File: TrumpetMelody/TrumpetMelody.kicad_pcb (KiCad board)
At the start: 2 copper layers, 76.2 x 68.6 mm, 81 parts, among them J1 USB_B_Micro, J2 Conn_01x05, J3 640456-3, J4 640456-3, SW1 SW_Push, U1 STM32F411RETx, U2 TLV62565DBVR, U3 MAX98357AETE_T, U4 MAX7375AXR805

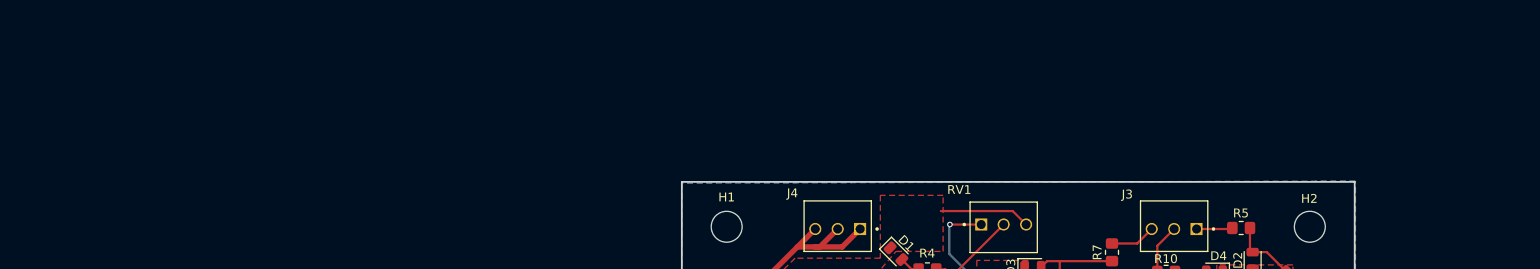
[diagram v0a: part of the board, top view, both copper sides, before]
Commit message: tbd list readded with things that need to be done
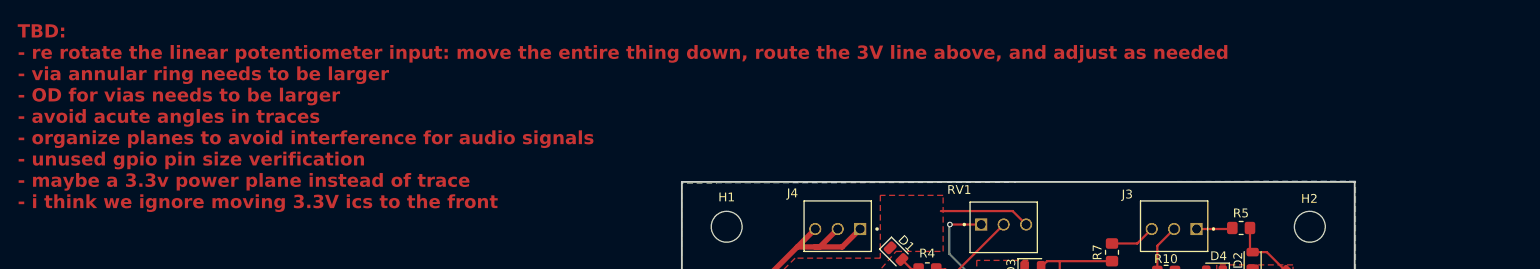
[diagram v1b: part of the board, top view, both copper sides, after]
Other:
- board text added: "TBD: - re rotate the linear potentiometer input: move the entire thing down, route the 3V line above, and adjust as needed - via annular ring needs to be larger - OD for vias needs to be larger - avoid acute angles in traces - organize planes to avoid interference for audio signals - unused gpio pin size verification - maybe a 3.3v power plane instead of trace - i think we ignore moving 3.3V ics 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"
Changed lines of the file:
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@@
   (gr_rect locked (start 147.32 45.72) (end 223.52 114.3)
     (stroke (width 0.2) (type default)) (fill none) (layer "Edge.Cuts"))
+  (gr_text "TBD:\n- re rotate the linear potentiometer input: move the entire thing down, route the 3V line above, and adjust as needed\n- via annular ring needs to be larger\n- OD for vias needs to be larger\n- avoid acute angles in traces\n- organize planes to avoid interference for audio signals\n- unused gpio pin size verification\n- maybe a 3.3v power plane instead of trace\n- i think we ignore moving 3.3V ics to the front" (at 72.105 48.87) (layer "F.Cu")
+    (effects (font (size 1.5 1.5) (thickness 0.3) bold) (justify left bottom))
+  )
   (gr_text "TMS" (at 185.301178 98.92878 -45) (layer "F.SilkS")
     (effects (font (size 0.635 0.635) (thickness 0.1)) (justify left bottom))

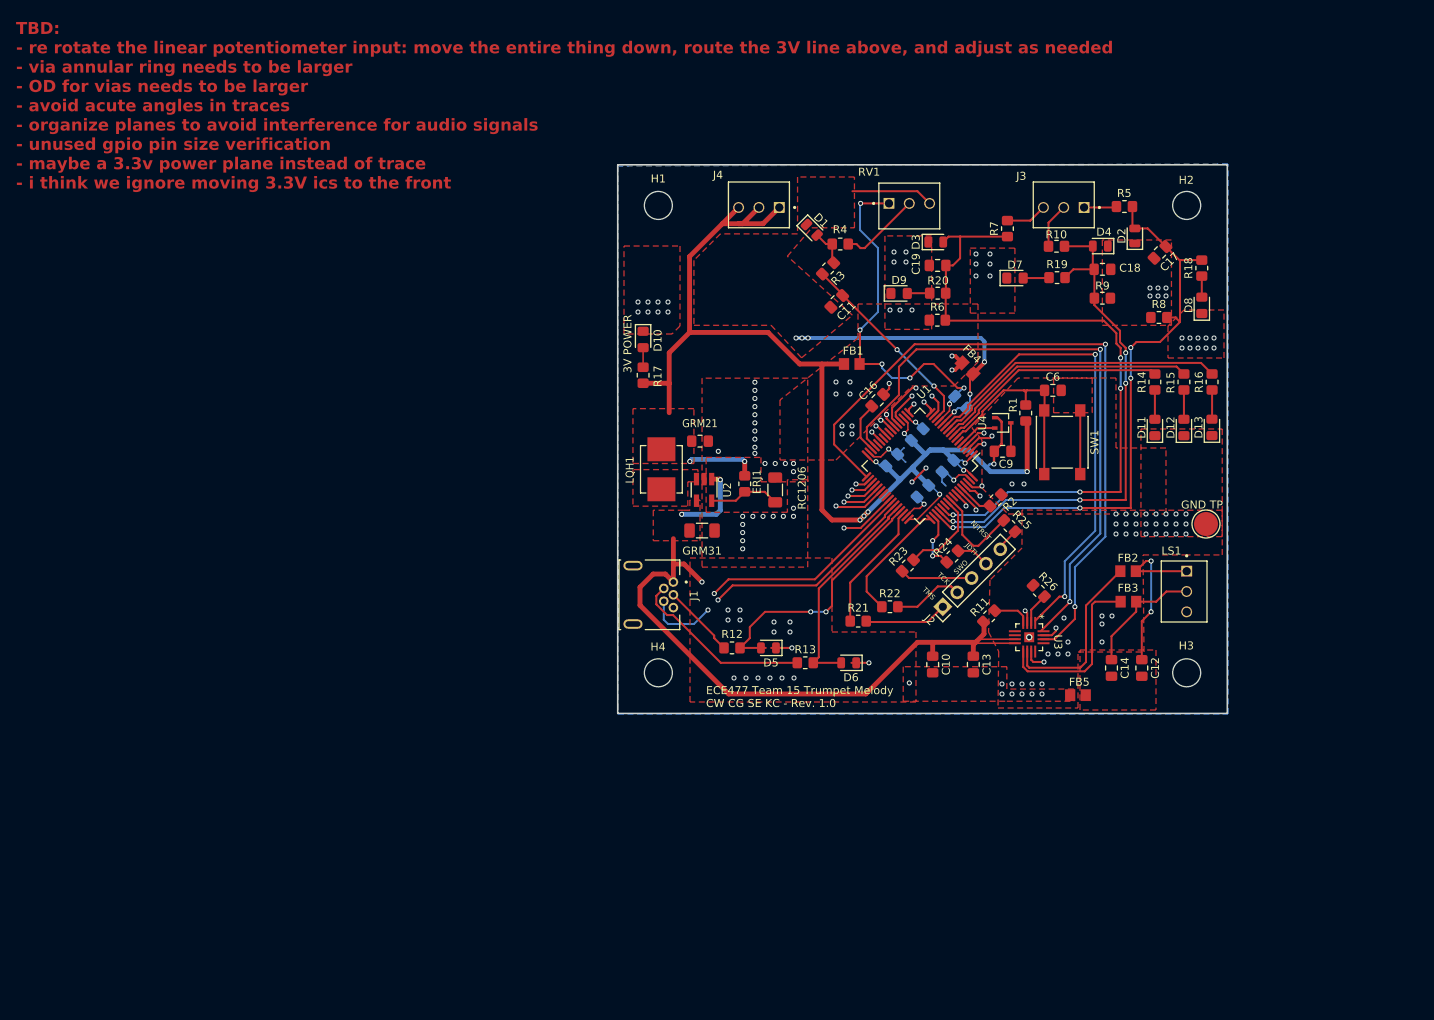
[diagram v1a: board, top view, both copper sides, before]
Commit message: modified the DRC rules based on jlcpcb minimums and DRC lit up like a christmas tree so i will be slowly going through that stuff
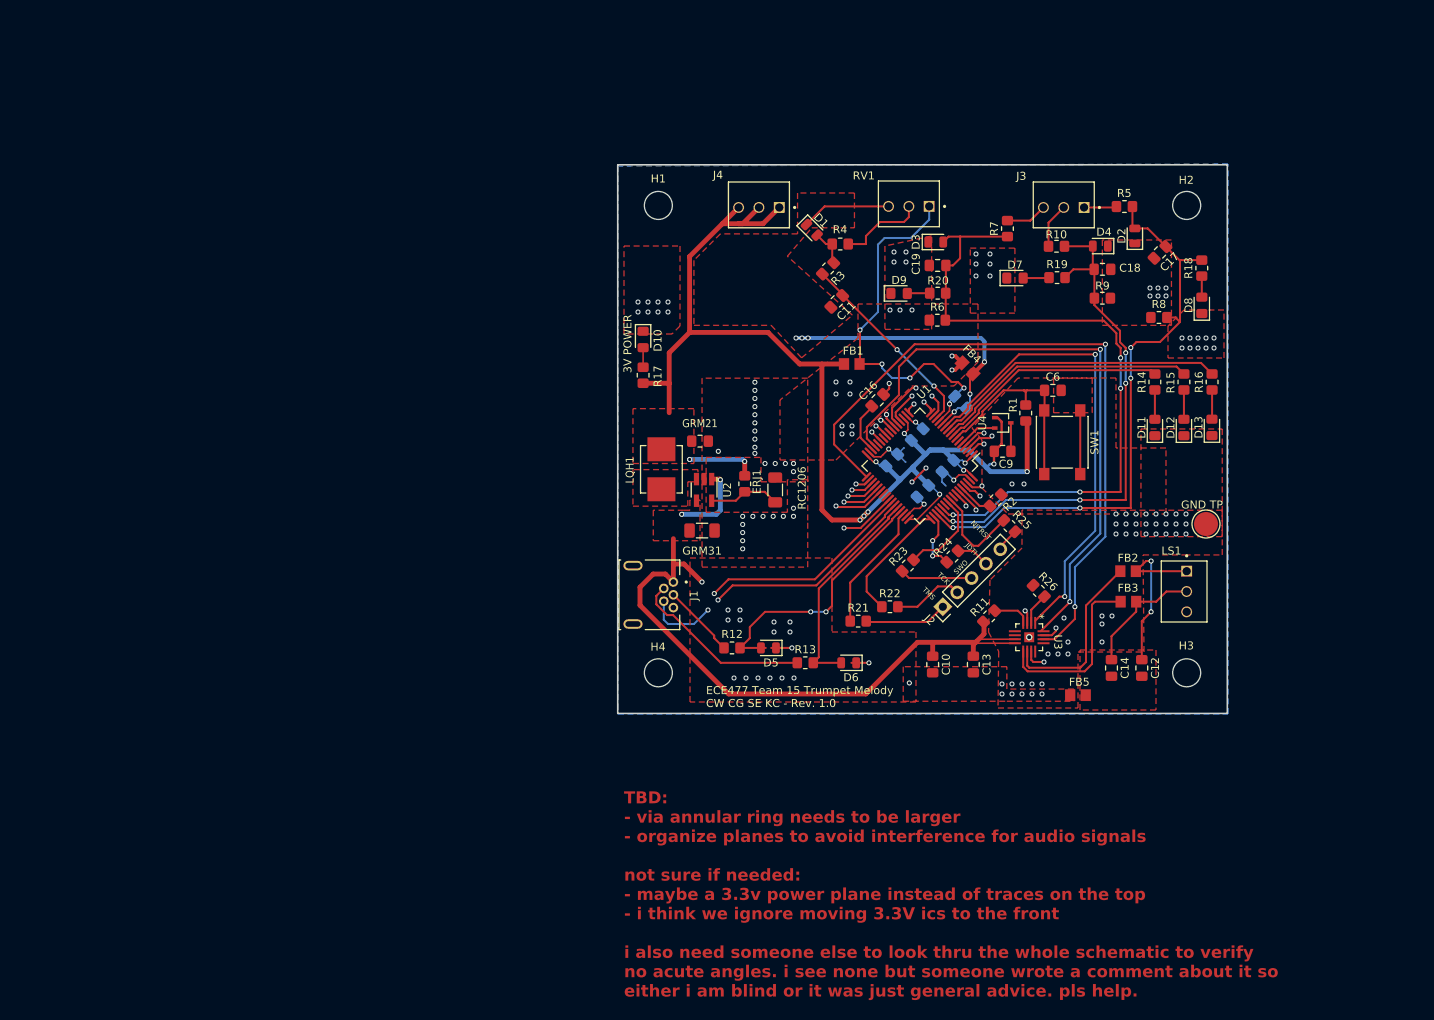
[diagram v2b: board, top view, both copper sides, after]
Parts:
- moved RV1 5.04 mm to (186.3, 50.9), turned to 0 degrees
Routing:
- net GNDA: track 47.1 -> 48.1 mm
- net Net-(R4-Pad2): track 10.2 -> 10.9 mm
- net +3.3VA: track 47.1 -> 46.8 mm, vias 6 -> 5
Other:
- board text added: "TBD: - via annular ring needs to be larger - organize planes to avoid interference for audio signals not sure if needed: - maybe a 3.3v power plane instead of traces on the top - i think we ignore moving 3.3V ics to the front i also need someone else to look thru the whole schematic to verify no acute angles. i see none but someone wrote a comment about it so either i am blind or it was just gene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"
- board text removed: "TBD: - re rotate the linear potentiometer input: move the entire thing down, route the 3V line above, and adjust as needed - via annular ring needs to be larger - OD for vias needs to be larger - avoid acute angles in traces - organize planes to avoid interference for audio signals - unused gpio pin size verification - maybe a 3.3v power plane instead of trace - i think we ignore moving 3.3V ics 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"

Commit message: christmas tree of DRC pointers
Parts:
- moved D13 0.19 mm to (221.8, 78.6)
- moved R16 0.12 mm to (221.7, 72.9)
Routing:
- net GPIO_LED2: track 37.3 -> 167.1 mm
- net GND: track 52.9 -> 52.0 mm
- net GNDA: track 48.1 -> 47.2 mm
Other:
- board text added: "TBD: - organize planes to avoid interference for audio signals not sure if needed: - maybe a 3.3v power plane instead of traces on the top - i think we ignore moving 3.3V ics to the front i also need someone else to look thru the whole schematic to verify no acute angles. i see none but someone wrote a comment about it so either i am blind or it was just general advice. pls help."
- board text removed: "TBD: - via annular ring needs to be larger - organize planes to avoid interference for audio signals not sure if needed: - maybe a 3.3v power plane instead of traces on the top - i think we ignore moving 3.3V ics to the front i also need someone else to look thru the whole schematic to verify no acute angles. i see none but someone wrote a comment about it so either i am blind or it was just gene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"

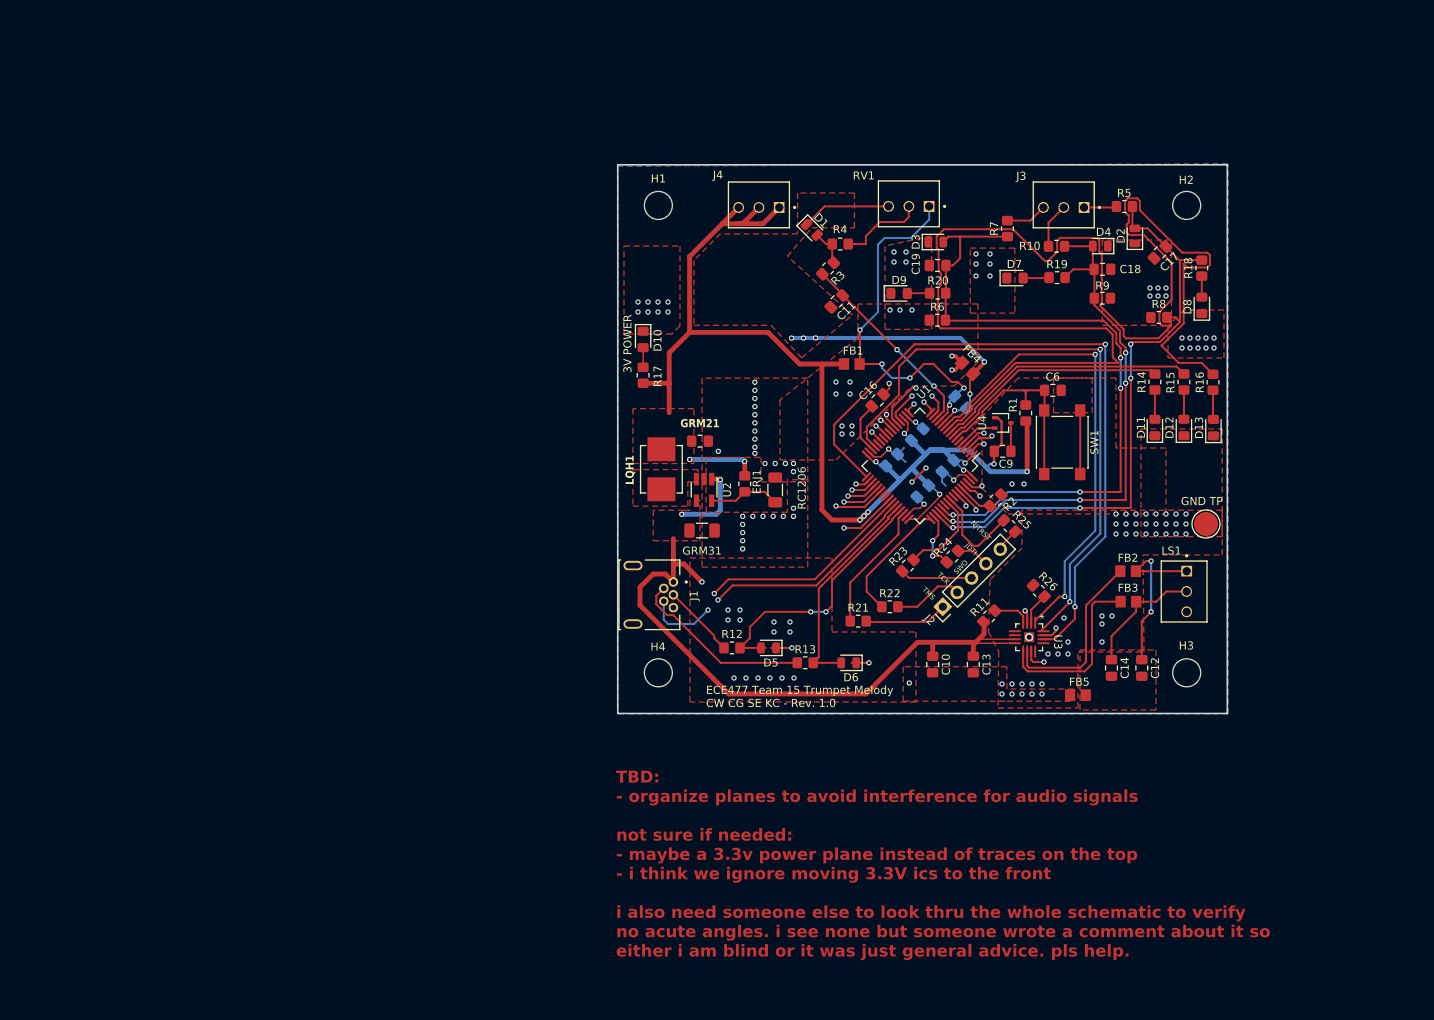
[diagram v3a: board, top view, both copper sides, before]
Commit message: finished DRC complaints pls verify the last warning ty
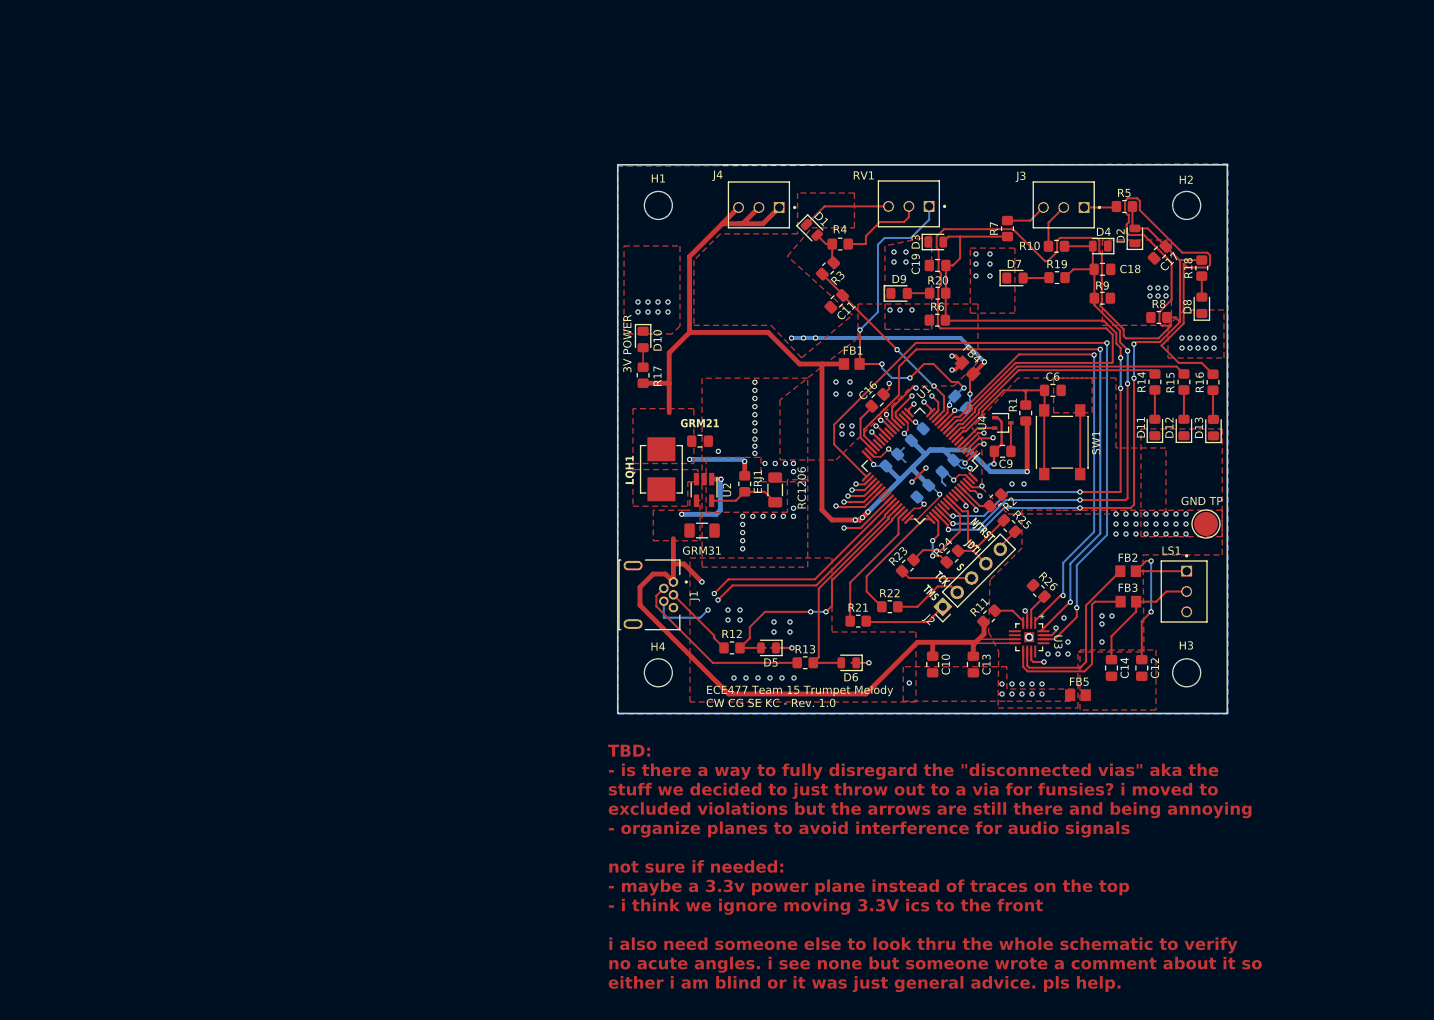
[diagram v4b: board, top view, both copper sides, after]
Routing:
- net GPIO_LED2: track 167.1 -> 166.0 mm
- net USB_ID_Connector: track 8.79 -> 7.97 mm
- net I2S_WS: track 87.5 -> 88.0 mm
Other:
- board text added: "S"
- board text added: "TBD: - is there a way to fully disregard the {dblquote}disconnected vias{dblquote} aka the stuff we decided to just throw out to a via for funsies? i moved to excluded violations but the arrows are still there and being annoying - organize planes to avoid interference for audio signals not sure if needed: - maybe a 3.3v power plane instead of traces on the top - i think we ignore moving 3.3V ics 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"
- board text removed: "SWO"
- board text removed: "TBD: - organize planes to avoid interference for audio signals not sure if needed: - maybe a 3.3v power plane instead of traces on the top - i think we ignore moving 3.3V ics to the front i also need someone else to look thru the whole schematic to verify no acute angles. i see none but someone wrote a comment about it so either i am blind or it was just general advice. pls help."
